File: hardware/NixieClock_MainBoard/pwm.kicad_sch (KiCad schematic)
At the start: 10 parts, among them U10 NC7SZ125M5X, U11 NC7SZ125M5X, U12 NC7SZ125M5X, U4 PCA9635, U5 NC7SZ125M5X, U7 NC7SZ125M5X, U8 NC7SZ125M5X, U9 NC7SZ125M5X

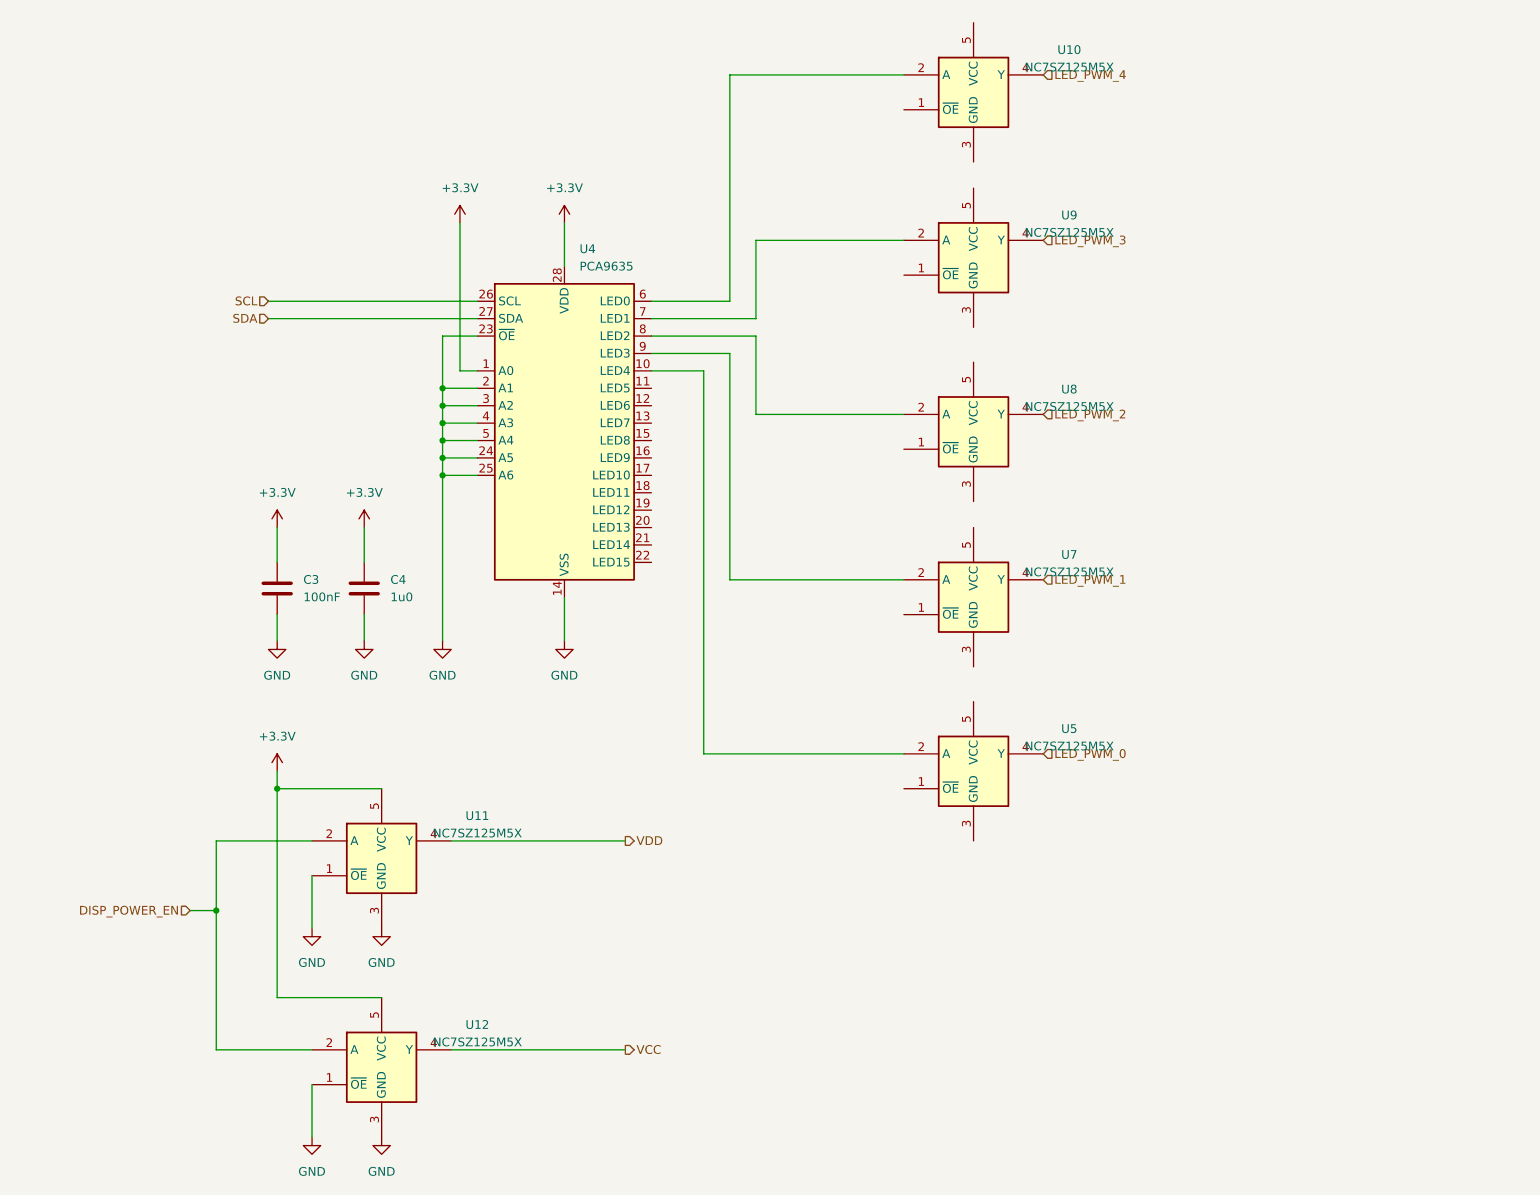
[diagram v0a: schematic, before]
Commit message: change sd card footprint changes on mainboard layout add stl files for display case
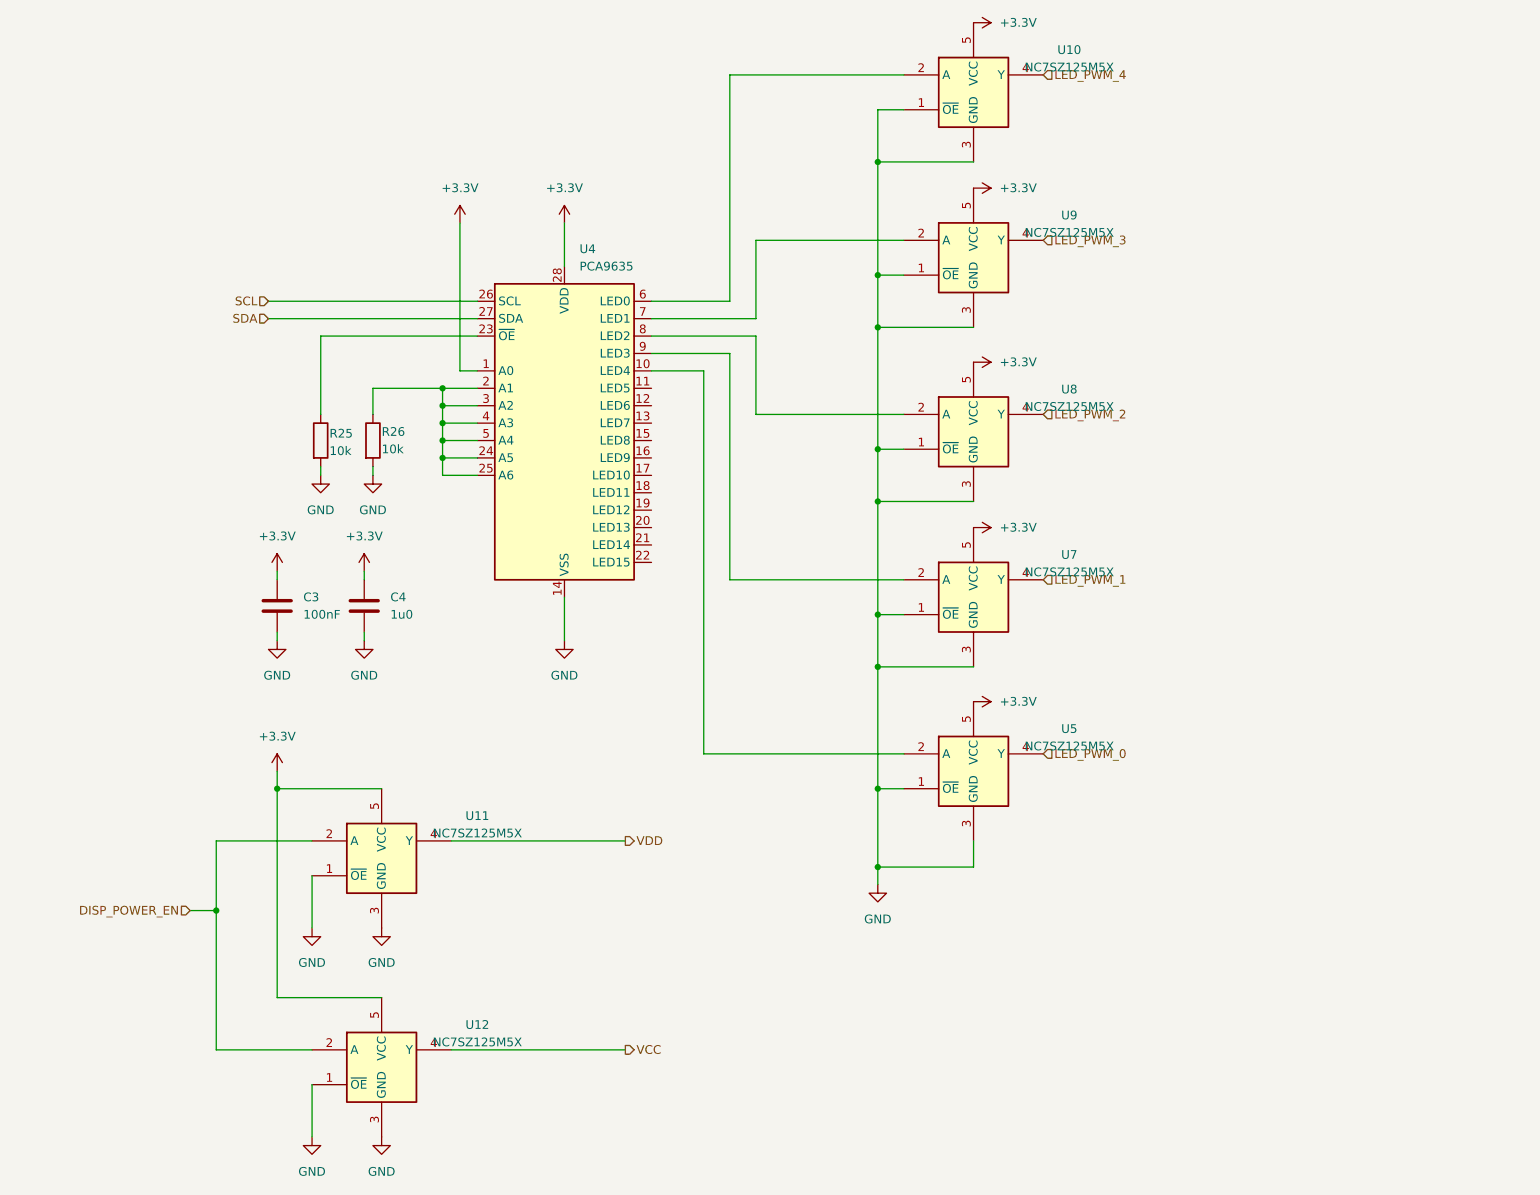
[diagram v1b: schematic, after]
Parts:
- added R25, R26: 10k, Resistor_SMD:R_0603_1608Metric, symbol Device:R
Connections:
- net +3.3V: now also U10.5 (VCC), U5.5 (VCC), U7.5 (VCC), U8.5 (VCC), U9.5 (VCC)
- net GND: now also U10.1 (~{OE}), U10.3 (GND), U5.1 (~{OE}), U5.3 (GND), U7.1 (~{OE}), U7.3 (GND), U8.1 (~{OE}), U8.3 (GND), U9.1 (~{OE}), U9.3 (GND), R25.2, R26.2; no longer U4.2 (A1), U4.23 (~{OE}), U4.24 (A5), U4.25 (A6), U4.3 (A2), U4.4 (A3), U4.5 (A4)
- new net: R26.1, U4.2 (A1), U4.24 (A5), U4.25 (A6), U4.3 (A2), U4.4 (A3), U4.5 (A4)
- new net: R25.1, U4.23 (~{OE})
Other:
- moved on the sheet: C3, C4

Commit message: V2.0 release fertig.
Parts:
- removed U11: NC7SZ125M5X, Package_TO_SOT_SMD:SOT-23-5, symbol 74xGxx:NC7SZ125M5X
- added C24, C25, C26, C27, C28: 1u0, Capacitor_SMD:C_0603_1608Metric, symbol Device:C
- added Q3: Si4532DY, Package_SO:SOIC-8_3.9x4.9mm_P1.27mm, symbol Transistor_FET:Si4532DY
- added R33, R34: 10k, Resistor_SMD:R_0603_1608Metric, symbol Device:R
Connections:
- net +3.3V: now also C24.1, C25.1, C26.1, C27.1, C28.1, Q3.3 (1), R34.1
- net DISP_POWER_EN: now also Q3.2 (G), R33.1
- net GND: now also C24.2, C25.2, C26.2, C27.2, C28.2, Q3.1 (S), R33.2
- net VDD: now also Q3.5 (D), Q3.6 (D)
- new net: Q3.4 (G), Q3.7 (D), Q3.8 (D), R34.2

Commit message: Version 2 Ready
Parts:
- removed Q3: Si4532DY, Package_SO:SOIC-8_3.9x4.9mm_P1.27mm, symbol Transistor_FET:Si4532DY
- added Q3: BSS123, Package_TO_SOT_SMD:SOT-23, symbol Transistor_FET:BSS123
- added Q4: Si2319CDS, Package_TO_SOT_SMD:SOT-23, symbol Transistor_FET:Si2319CDS
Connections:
- net +3.3V: now also Q4.2 (S)
- net DISP_POWER_EN: now also Q3.1 (G)
- net GND: now also Q3.2 (S)
- net VDD: now also Q4.3 (D)
- net at R34.2: now also Q3.3 (D), Q4.1 (G)
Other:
- note added: "SI2399DS-T1-GE3"
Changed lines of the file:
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@@
 		)
 	)
+	(text "SI2399DS-T1-GE3"
+		(exclude_from_sim no)
+		(at 115.316 138.176 0)
+		(effects
+			(font
+				(size 1.27 1.27)
+			)
+		)
+	)
 	(hierarchical_label "VCC"
 		(shape output)
@@
 	)
 	(symbol
+		(lib_id "Transistor_FET:BSS123")
+		(at 114.3 162.56 0)
+		(unit 1)
+		(exclude_from_sim no)
+		(in_bom yes)
+		(on_board yes)
+		(dnp no)
+		(fields_autoplaced yes)
+		(property "Reference" "Q3"
+			(at 120.65 161.2899 0)
+			(effects
+				(font
+					(size 1.27 1.27)
+				)
+				(justify left)
+			)
+		)
+		(property "Value" "BSS123"
+			(at 120.65 163.8299 0)
+			(effects
+				(font
+					(size 1.27 1.27)
+				)
+				(justify left)
+			)
+		)
+		(property "Footprint" "Package_TO_SOT_SMD:SOT-23"
+			(at 119.38 164.465 0)
+			(effects
+				(font
+					(size 1.27 1.27)
+					(italic yes)
+				)
+				(justify left)
+				(hide yes)
+			)
+		)
+		(property "Datasheet" "http://www.diodes.com/assets/Datasheets/ds30366.pdf"
+			(at 119.38 166.37 0)
+			(effects
+				(font
+					(size 1.27 1.27)
+				)
+				(justify left)
+				(hide yes)
+			)
+		)
+		(property "Description" "0.17A Id, 100V Vds, N-Channel MOSFET, SOT-23"
+			(at 114.3 162.56 0)
+			(effects
+				(font
+					(size 1.27 1.27)
+				)
+				(hide yes)
+			)
+		)
+		(pin "3"
+		)
+		(pin "2"
+		)
+		(pin "1"
+		)
+		(instances
+			(project ""
+				(path "/5ddb5910-d1ea-4e23-971a-19156fc3bbe9/e1d3402d-a317-4c73-b48d-1dbf4ee272dd"
+					(reference "Q3")
+					(unit 1)
+				)
+			)
+		)
+	)
+	(symbol
 		(lib_id "power:GND")
 		(at 81.28 190.5 0)
@@
 	)
 	(symbol
+		(lib_id "Transistor_FET:Si2319CDS")
+		(at 116.84 149.86 270)
+		(mirror x)
+		(unit 1)
+		(exclude_from_sim no)
+		(in_bom yes)
+		(on_board yes)
+		(dnp no)
+		(fields_autoplaced yes)
+		(property "Reference" "Q4"
+			(at 116.84 140.97 90)
+			(effects
+				(font
+					(size 1.27 1.27)
+				)
+			)
+		)
+		(property "Value" "Si2319CDS"
+			(at 116.84 143.51 90)
+			(effects
+				(font
+					(size 1.27 1.27)
+				)
+			)
+		)
+		(property "Footprint" "Package_TO_SOT_SMD:SOT-23"
+			(at 114.935 144.78 0)
+			(effects
+				(font
+					(size 1.27 1.27)
+					(italic yes)
+				)
+				(justify left)
+				(hide yes)
+			)
+		)
+		(property "Datasheet" "http://www.vishay.com/docs/66709/si2319cd.pdf"
+			(at 113.03 144.78 0)
+			(effects
+				(font
+					(size 1.27 1.27)
+				)
+				(justify left)
+				(hide yes)
+			)
+		)
+		(property "Description" "-4.4A Id, -40V Vds, P-Channel MOSFET, SOT-23"
+			(at 116.84 149.86 0)
+			(effects
+				(font
+					(size 1.27 1.27)
+				)
+				(hide yes)
+			)
+		)
+		(pin "3"
+		)
+		(pin "2"
+		)
+		(pin "1"
+		)
+		(instances
+			(project ""
+				(path "/5ddb5910-d1ea-4e23-971a-19156fc3bbe9/e1d3402d-a317-4c73-b48d-1dbf4ee272dd"
+					(reference "Q4")
+					(unit 1)
+				)
+			)
+		)
+	)
+	(symbol
 		(lib_id "power:GND")
 		(at 118.11 118.11 0)
@@
 	)
 	(symbol
-		(lib_id "Transistor_FET:Si4532DY")
-		(at 114.3 162.56 0)
-		(unit 1)
-		(exclude_from_sim no)
-		(in_bom yes)
-		(on_board yes)
-		(dnp no)
-		(fields_autoplaced yes)
-		(property "Reference" "Q3"
-			(at 120.65 161.2899 0)
-			(effects
-				(font
-					(size 1.27 1.27)
-				)
-				(justify left)
-			)
-		)
-		(property "Value" "Si4532DY"
-			(at 120.65 163.8299 0)
-			(effects
-				(font
-					(size 1.27 1.27)
-				)
-				(justify left)
-			)
-		)
-		(property "Footprint" "Package_SO:SOIC-8_3.9x4.9mm_P1.27mm"
-			(at 119.38 164.465 0)
-			(effects
-				(font
-					(size 1.27 1.27)
-					(italic yes)
-				)
-				(justify left)
-				(hide yes)
-			)
-		)
-		(property "Datasheet" "https://www.onsemi.com/pub/Collateral/SI4532DY-D.PDF"
-			(at 119.38 166.37 0)
-			(effects
-				(font
-					(size 1.27 1.27)
-				)
-				(justify left)
-				(hide yes)
-			)
-		)
-		(property "Description" "3.9A Id, 30V Vds, Dual N and P Channel MOSFET, 65mOhm Ron, 10V Vgs, SO8L"
-			(at 114.3 162.56 0)
-			(effects
-				(font
-					(size 1.27 1.27)
-				)
-				(hide yes)
-			)
-		)
-		(pin "7"
-		)
-		(pin "1"
-		)
-		(pin "5"
-		)
-		(pin "2"
-		)
-		(pin "4"
-		)
-		(pin "3"
-		)
-		(pin "6"
-		)
-		(pin "8"
-		)
-		(instances
-			(project ""
-				(path "/5ddb5910-d1ea-4e23-971a-19156fc3bbe9/e1d3402d-a317-4c73-b48d-1dbf4ee272dd"
-					(reference "Q3")
-					(unit 1)
-				)
-			)
-		)
-	)
-	(symbol
 		(lib_id "power:+3.3V")
 		(at 177.8 52.07 270)
@@
 				)
 			)
-		)
-	)
-	(symbol
-		(lib_id "Transistor_FET:Si4532DY")
-		(at 116.84 149.86 270)
-		(mirror x)
-		(unit 2)
-		(exclude_from_sim no)
-		(in_bom yes)
-		(on_board yes)
-		(dnp no)
-		(property "Reference" "Q3"
-			(at 116.84 140.97 90)
-			(effects
-				(font
-					(size 1.27 1.27)
-				)
-			)
-		)
-		(property "Value" "Si4532DY"
-			(at 116.84 143.51 90)
-			(effects
-				(font
-					(size 1.27 1.27)
-				)
-			)
-		)
-		(property "Footprint" "Package_SO:SOIC-8_3.9x4.9mm_P1.27mm"
-			(at 114.935 144.78 0)
-			(effects
-				(font
-					(size 1.27 1.27)
-					(italic yes)
-				)
-				(justify left)
-				(hide yes)
-			)
-		)
-		(property "Datasheet" "https://www.onsemi.com/pub/Collateral/SI4532DY-D.PDF"
-			(at 113.03 144.78 0)
-			(effects
-				(font
-					(size 1.27 1.27)
-				)
-				(justify left)
-				(hide yes)
-			)
-		)
-		(property "Description" "3.9A Id, 30V Vds, Dual N and P Channel MOSFET, 65mOhm Ron, 10V Vgs, SO8L"
-			(at 116.84 149.86 0)
-			(effects
-				(font
-					(size 1.27 1.27)
-				)
-				(hide yes)
-			)
-		)
-		(pin "7"
-		)
-		(pin "1"
-		)
-		(pin "5"
-		)
-		(pin "2"
-		)
-		(pin "4"
-		)
-		(pin "3"
-		)
-		(pin "6"
-		)
-		(pin "8"
-		)
-		(instances
-			(project ""
-				(path "/5ddb5910-d1ea-4e23-971a-19156fc3bbe9/e1d3402d-a317-4c73-b48d-1dbf4ee272dd"
-					(reference "Q3")
-					(unit 2)
-				)
-			)
